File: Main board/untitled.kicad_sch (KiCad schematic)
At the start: 15 parts, among them U2 BMI088, U3 MS5607-02BA03, U4 ADXL375BCCZ-RL7, U5 SN74LVC1G32MDBVREP

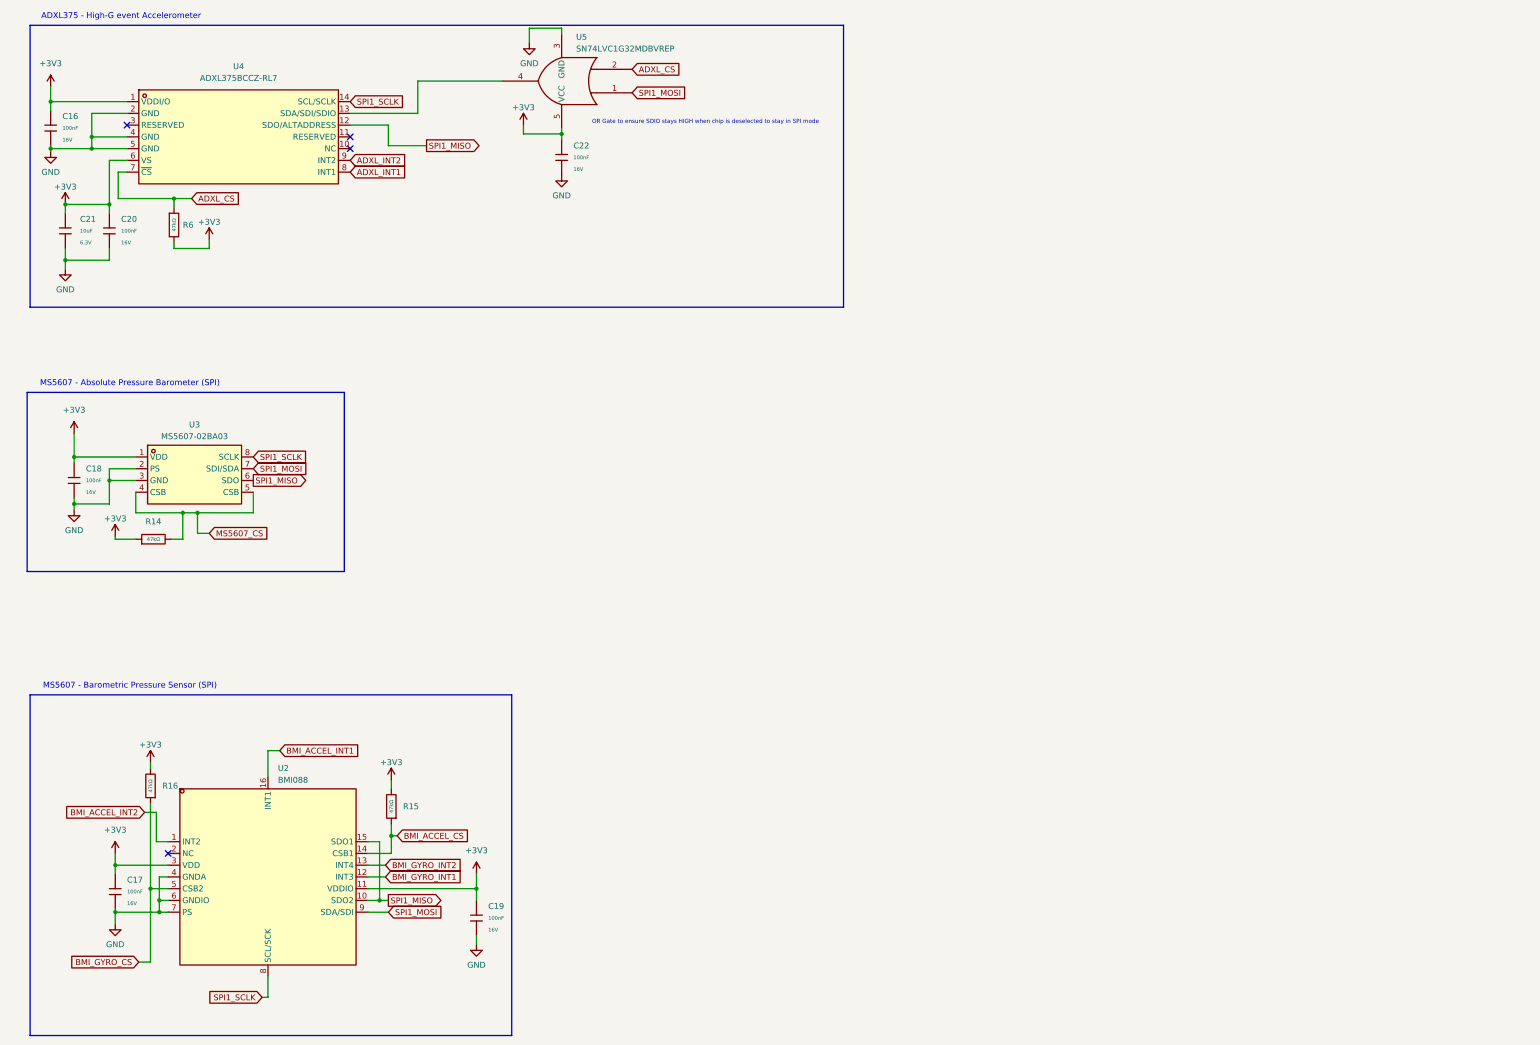
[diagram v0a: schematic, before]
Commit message: Changed to single-board architecture
SPI Layout #1. Shared bus close to USB D+-, might be bad for layout later.
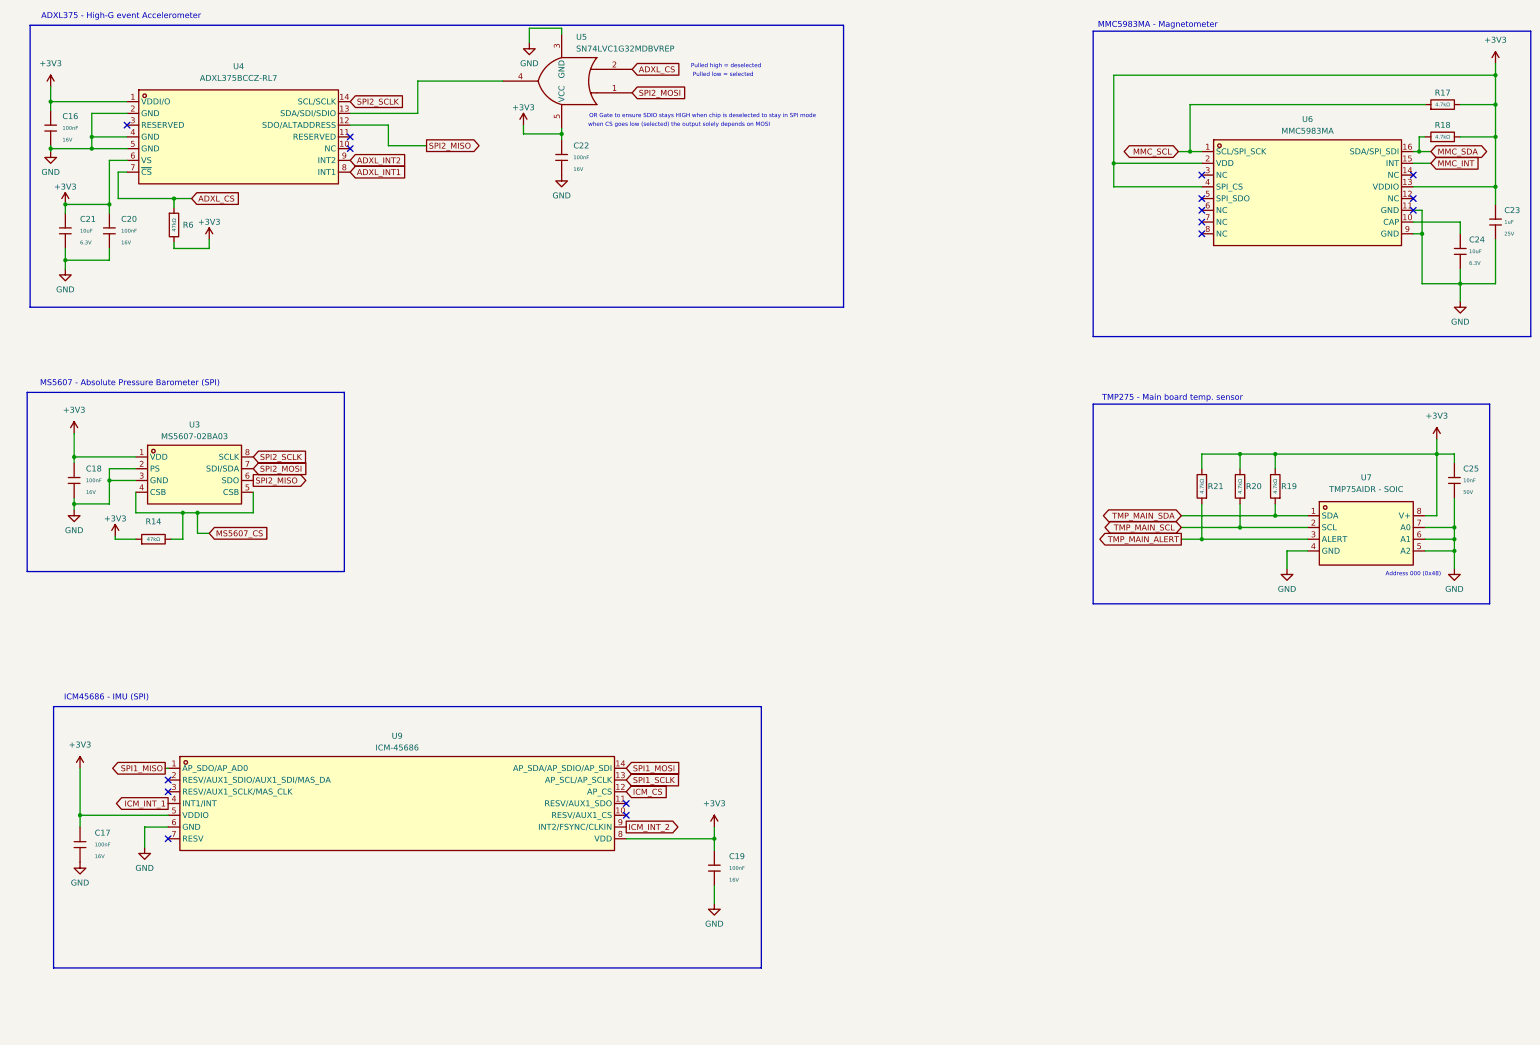
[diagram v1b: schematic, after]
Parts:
- removed R15, R16: 47kΩ, PCM_JLCPCB:R_0402, symbol PCM_JLCPCB-Resistors:0402,47kΩ
- removed U2: BMI088, EasyEDA:LGA-16_L4.5-W3.0-P0.50-BL, symbol EasyEDA:BMI088
- added C23: 1uF, PCM_JLCPCB:C_0402, symbol PCM_JLCPCB-Capacitors:0402,1uF
- added C24: 10uF, PCM_JLCPCB:C_0402, symbol PCM_JLCPCB-Capacitors:0402,10uF
- added C25: 10nF, PCM_JLCPCB:C_0402, symbol PCM_JLCPCB-Capacitors:0402,10nF
- added R17, R18, R19, R20, R21: 4.7kΩ, PCM_JLCPCB:R_0402, symbol PCM_JLCPCB-Resistors:0402,4.7kΩ
- added U6: MMC5983MA, EasyEDA:LGA-16_L3.0-W3.0-P0.50-BL_SQ, symbol EasyEDA:MMC5983MA
- added U7: TMP75AIDR - SOIC, EasyEDA:SOIC-8_L4.9-W3.9-P1.27-LS6.0-BL, symbol EasyEDA:TMP75AIDR
- added U9: ICM-45686, EasyEDA:LGA-14_L3.0-W2.5-P0.50-TL, symbol EasyEDA:ICM-45686
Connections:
- net +3V3: now also C23.1, C25.1, R17.2, R18.2, R19.2, R20.2, R21.2, U6.13 (VDDIO), U6.2 (VDD), U6.4 (SPI_CS), U7.8 (V+), U9.5 (VDDIO), U9.8 (VDD)
- net GND: now also C23.2, C24.2, C25.2, U6.11 (GND), U6.9 (GND), U7.4 (GND), U7.5 (A2), U7.6 (A1), U7.7 (A0), U9.6 (GND)
- net SPI1_MISO: now also U9.1 (AP_SDO/AP_AD0); no longer U3.6 (SDO), U4.12 (SDO/ALTADDRESS)
- net SPI1_MOSI: now also U9.14 (AP_SDA/AP_SDIO/AP_SDI); no longer U3.7 (SDI/SDA), U5.1
- net SPI1_SCLK: now also U9.13 (AP_SCL/AP_SCLK); no longer U3.8 (SCLK), U4.14 (SCL/SCLK)
- new net: C24.1, U6.10 (CAP)
- new net ICM_CS: U9.12 (AP_CS)
- new net ICM_INT_1: U9.4 (INT1/INT)
- new net ICM_INT_2: U9.9 (INT2/FSYNC/CLKIN)
- new net MMC_INT: U6.15 (INT)
- new net MMC_SCL: R17.1, U6.1 (SCL/SPI_SCK)
- new net MMC_SDA: R18.1, U6.16 (SDA/SPI_SDI)
- new net SPI2_MISO: U3.6 (SDO), U4.12 (SDO/ALTADDRESS)
- new net SPI2_MOSI: U3.7 (SDI/SDA), U5.1
- new net SPI2_SCLK: U3.8 (SCLK), U4.14 (SCL/SCLK)
- new net TMP_MAIN_ALERT: R21.1, U7.3 (ALERT)
- new net TMP_MAIN_SCL: R20.1, U7.2 (SCL)
- new net TMP_MAIN_SDA: R19.1, U7.1 (SDA)
- no-connect marks 4 -> 16
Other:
- note added: "Address 000 (0x48)"
- note added: "ICM45686 - IMU (SPI)"
- note added: "MMC5983MA - Magnetometer"
- note added: "Pulled high = deselected"
- note added: "Pulled low = selected"
- note added: "TMP275 - Main board temp. sensor"
- note added: "when CS goes low (selected) the output solely depends on MOSI"
- note removed: "MS5607 - Barometric Pressure Sensor (SPI)"

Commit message: Schematics completed + layout
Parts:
- removed C25: 10nF, PCM_JLCPCB:C_0402, symbol PCM_JLCPCB-Capacitors:0402,10nF
- removed R19, R20, R21: 4.7kΩ, PCM_JLCPCB:R_0402, symbol PCM_JLCPCB-Resistors:0402,4.7kΩ
- removed U7: TMP75AIDR - SOIC, EasyEDA:SOIC-8_L4.9-W3.9-P1.27-LS6.0-BL, symbol EasyEDA:TMP75AIDR
- added R31: 10kΩ, PCM_JLCPCB:R_0402, symbol PCM_JLCPCB-Resistors:0402,10kΩ
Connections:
- net +3V3: now also R31.2
- net ADXL_INT2: no longer names the net of U4.9 (INT2)
- net ICM_INT_2: no longer names the net of U9.9 (INT2/FSYNC/CLKIN)
- net ICM_INT_2: now also R31.1
- no-connect marks 16 -> 17
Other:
- note removed: "Address 000 (0x48)"
- note removed: "TMP275 - Main board temp. sensor"

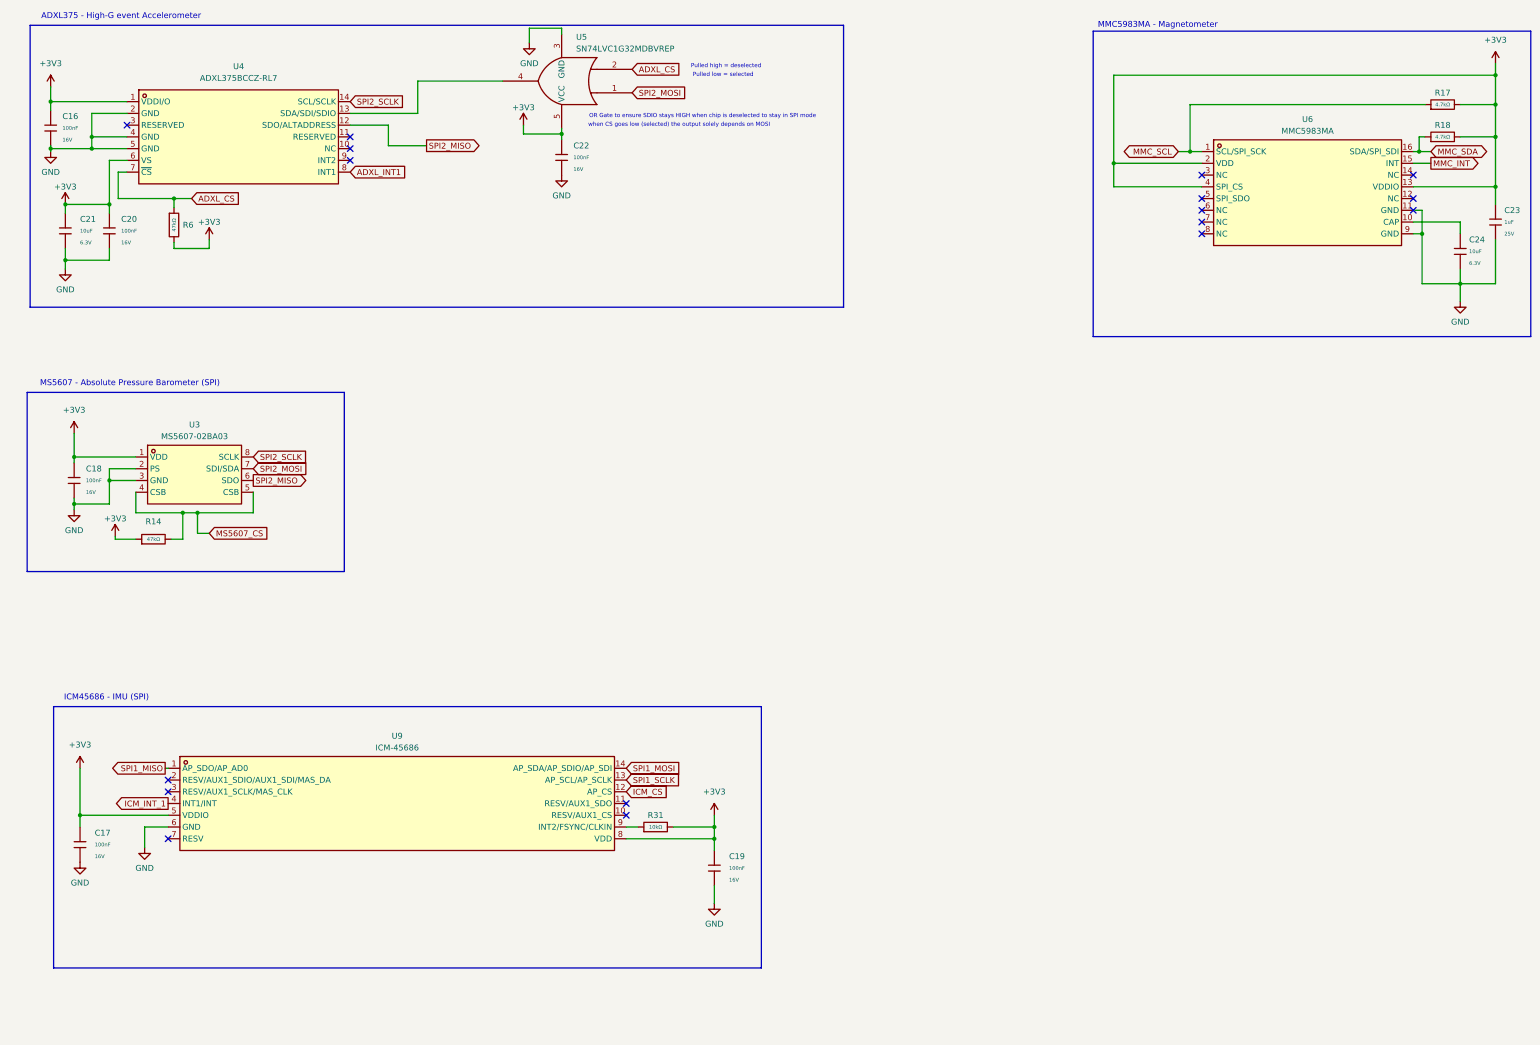
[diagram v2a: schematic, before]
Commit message: Final Layout (Pre-silkscreen)
- Added  1M resistors in parallel with the igniters for static dissipation
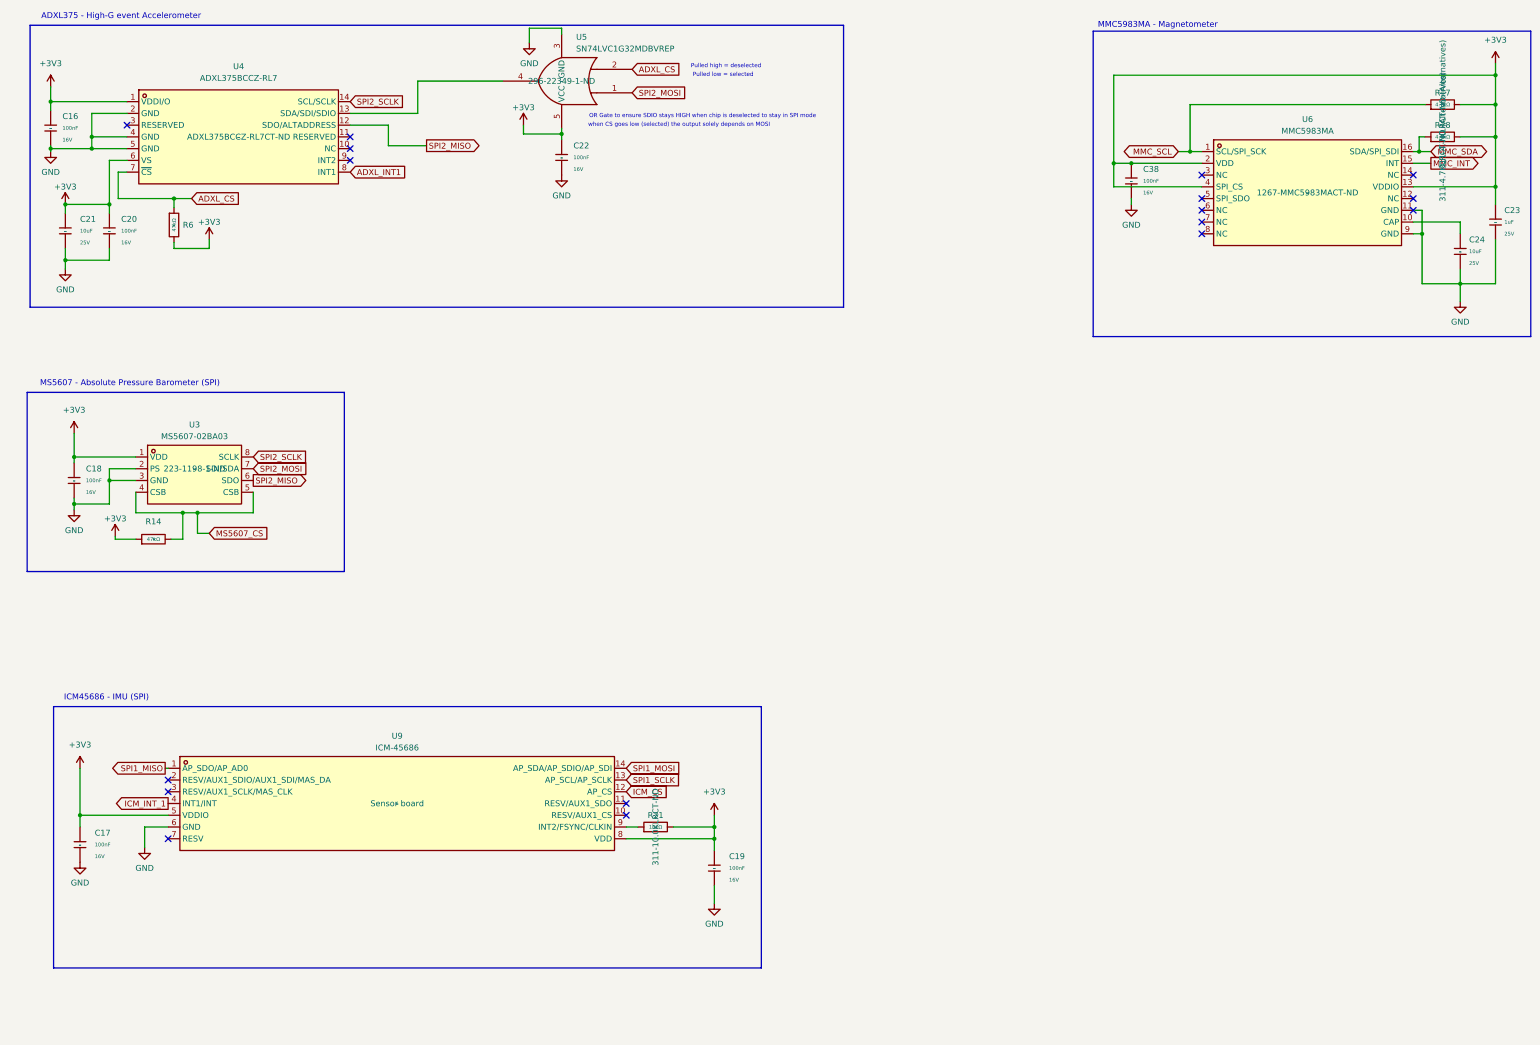
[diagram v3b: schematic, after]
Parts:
- added C38: 100nF, PCM_JLCPCB:C_0402, symbol PCM_JLCPCB-Capacitors:0402,100nF
- C16, C17, C18, C19, C20, C22, C23, R14, R6: Aliexpress (none) -> -; Digikey Part No. (none) -> -
- C21, C24: footprint PCM_JLCPCB:C_0402 -> PCM_JLCPCB:C_0603; Aliexpress (none) -> -; Digikey Part No. (none) -> -; LCSC C15525 -> C96446; Voltage Rated 6.3V -> 25V
- R17, R18: Aliexpress (none) -> -; Digikey Part No. (none) -> 311-4.7KLRCT-ND (Alternatives); LCSC C25900 -> C25900 (OUT OF STOCK)
- R31: Aliexpress (none) -> -; Digikey Part No. (none) -> 311-10.0KLRCT-ND; LCSC C25744 -> C25744 (OUT OF STOCK)
- U3: footprint EasyEDA:SENSOR-SMD_MS560702BA03-50 -> EASYEDA:SENSOR-SMD_MS560702BA03-50; Aliexpress (none) -> -; Digikey Part No. (none) -> 223-1198-1-ND; LCSC (none) -> -
- U4: footprint EasyEDA:LGA-14_L5.0-W3.0-P0.80-BL -> EASYEDA:LGA-14_L5.0-W3.0-P0.80-BL; Aliexpress (none) -> -; Digikey Part No. (none) -> ADXL375BCCZ-RL7CT-ND; LCSC (none) -> -
- U5: Aliexpress (none) -> -; Digikey Part No. (none) -> 296-22349-1-ND; LCSC (none) -> -
- U6: footprint EasyEDA:LGA-16_L3.0-W3.0-P0.50-BL_SQ -> EASYEDA:LGA-16_L3.0-W3.0-P0.50-BL_SQ; Aliexpress (none) -> -; Digikey Part No. (none) -> 1267-MMC5983MACT-ND; LCSC (none) -> -
- U9: footprint EasyEDA:LGA-14_L3.0-W2.5-P0.50-TL -> EASYEDA:LGA-14_L3.0-W2.5-P0.50-TL; Aliexpress (none) -> Sensor board; Digikey Part No. (none) -> -; LCSC (none) -> -
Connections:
- net +3V3: now also C38.1
- net GND: now also C38.2

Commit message: Included IMU project
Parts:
- added U8: MS5607-02BA03, EasyEDA:SENSOR-SMD_MS560702BA03-50, symbol EASYEDA:MS5607-02BA03
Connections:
- no-connect marks 17 -> 16
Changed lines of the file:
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@@
 	)
 	(no_connect
-		(at 318.135 70.485)
-	)
-	(no_connect
 		(at 147.955 201.295)
 	)
@@
 		)
 		(property "Digikey Part No." "311-10.0KLRCT-ND"
-			(at 154.305 203.835 0)
+			(at 154.94 210.82 90)
 			(effects
 				(font
@@
 					(unit 1)
 				)
+			)
+		)
+	)
+	(symbol
+		(lib_id "EASYEDA:MS5607-02BA03")
+		(at 215.9 121.285 0)
+		(unit 1)
+		(exclude_from_sim no)
+		(in_bom yes)
+		(on_board yes)
+		(dnp no)
+		(fields_autoplaced yes)
+		(property "Reference" "U8"
+			(at 215.9 111.76 0)
+			(effects
+				(font
+					(size 1.27 1.27)
+				)
+			)
+		)
+		(property "Value" "MS5607-02BA03"
+			(at 215.9 114.3 0)
+			(effects
+				(font
+					(size 1.27 1.27)
+				)
+			)
+		)
+		(property "Footprint" "EasyEDA:SENSOR-SMD_MS560702BA03-50"
+			(at 215.9 133.985 0)
+			(effects
+				(font
+					(size 1.27 1.27)
+				)
+				(hide yes)
+			)
+		)
+		(property "Datasheet" ""
+			(at 215.9 121.285 0)
+			(effects
+				(font
+					(size 1.27 1.27)
+				)
+				(hide yes)
+			)
+		)
+		(property "Description" ""
+			(at 215.9 121.285 0)
+			(effects
+				(font
+					(size 1.27 1.27)
+				)
+				(hide yes)
+			)
+		)
+		(property "LCSC Part" "C9900023641"
+			(at 215.9 136.525 0)
+			(effects
+				(font
+					(size 1.27 1.27)
+				)
+				(hide yes)
+			)
+		)
+		(pin "1"
+		)
+		(pin "3"
+		)
+		(pin "2"
+		)
+		(pin "4"
+		)
+		(pin "8"
+		)
+		(pin "7"
+		)
+		(pin "6"
+		)
+		(pin "5"
+		)
+		(instances
+			(project ""
+				(path "/1f0f75a1-1d31-43c9-b0ad-8555040f61e7/e2fd82b4-49f6-453e-97db-cfd425c520a6"
+					(reference "U8")
+					(unit 1)
+				)
